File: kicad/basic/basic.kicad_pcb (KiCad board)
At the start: 2 copper layers, 50 x 50 mm, 20 parts, among them P2 CONN_01X15, P3 CONN_01X15, P4 CONN_01X06, P5 CONN_01X01, P6 CONN_01X01, P7 CONN_01X01, P8 CONN_01X01, P9 CONN_01X06, SW1 SW_PUSH, SW2 SW_PUSH

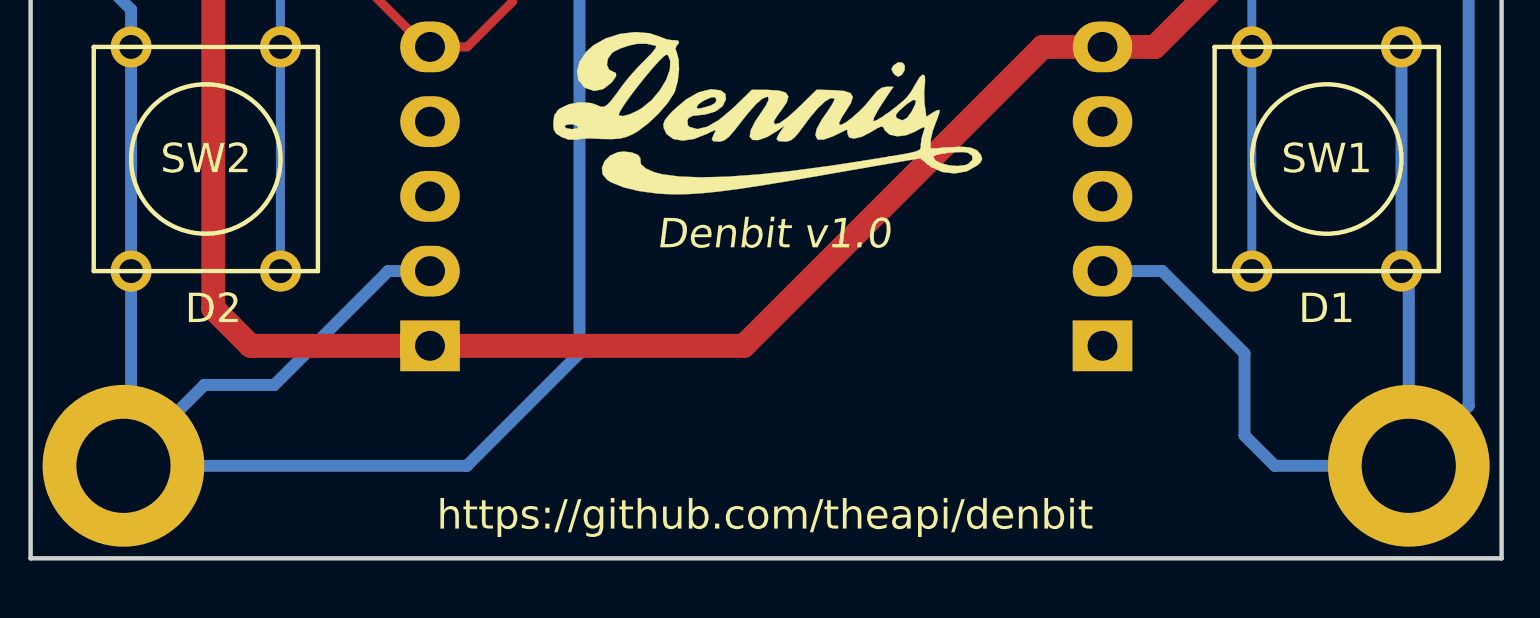
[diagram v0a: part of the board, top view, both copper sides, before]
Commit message: Switch silkscreen labels
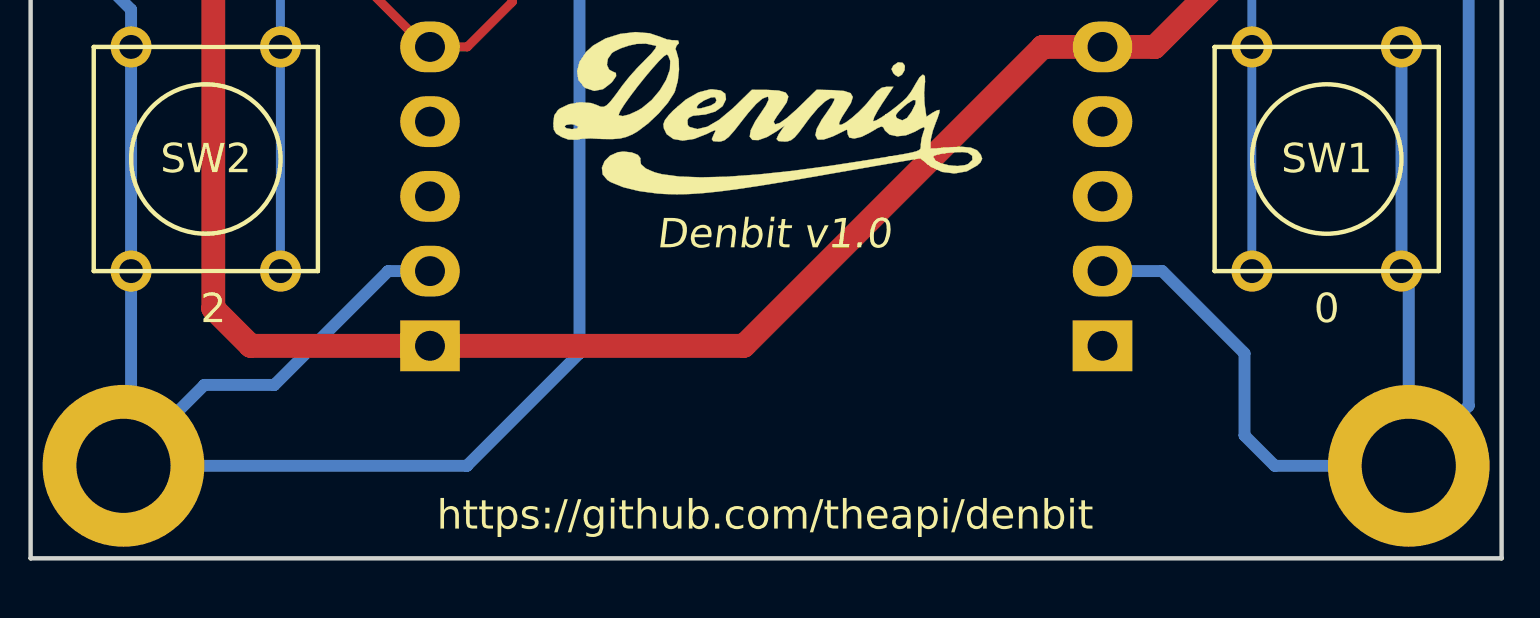
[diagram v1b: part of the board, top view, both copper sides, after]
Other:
- board text added: "0"
- board text added: "2"
- board text removed: "D1"
- board text removed: "D2"
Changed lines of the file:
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@@
     (links 41)
     (no_connects 0)
-    (area 120.251999 71.737999 170.402001 121.888001)
+    (area 115.226999 66.712999 175.427001 126.913001)
     (thickness 1.6)
     (drawings 73)
@@
   (gr_line (start 148.888 72.426) (end 147.872 72.426) (angle 90) (layer B.SilkS) (width 0.2))
   (gr_line (start 148.888 76.998) (end 148.888 72.426) (angle 90) (layer B.SilkS) (width 0.2))
-  (gr_text D2 (at 126.536 113.32) (layer F.SilkS)
+  (gr_text 2 (at 126.536 113.32) (layer F.SilkS)
     (effects (font (size 1 1) (thickness 0.15)))
   )
-  (gr_text D1 (at 164.382 113.32) (layer F.SilkS)
+  (gr_text 0 (at 164.382 113.32) (layer F.SilkS)
     (effects (font (size 1 1) (thickness 0.15)))
   )

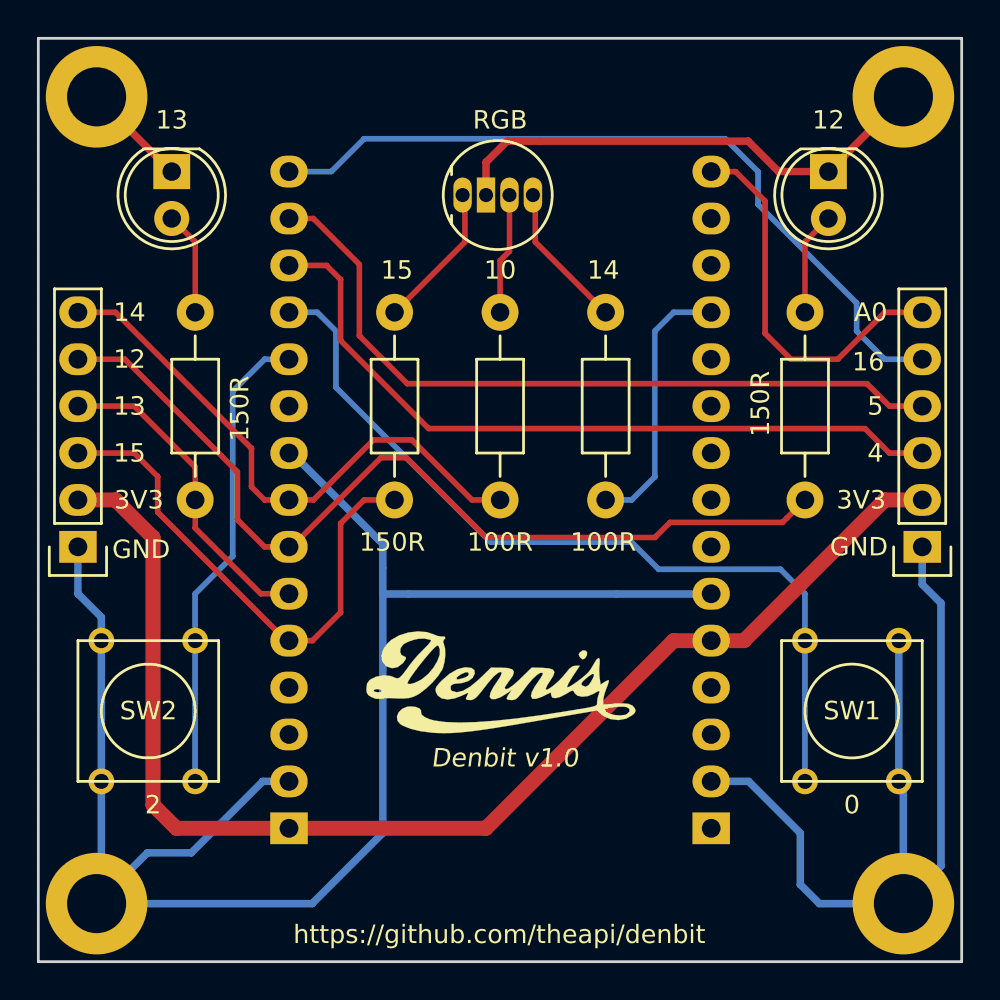
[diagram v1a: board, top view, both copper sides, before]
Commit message: Connect the right switch to the header
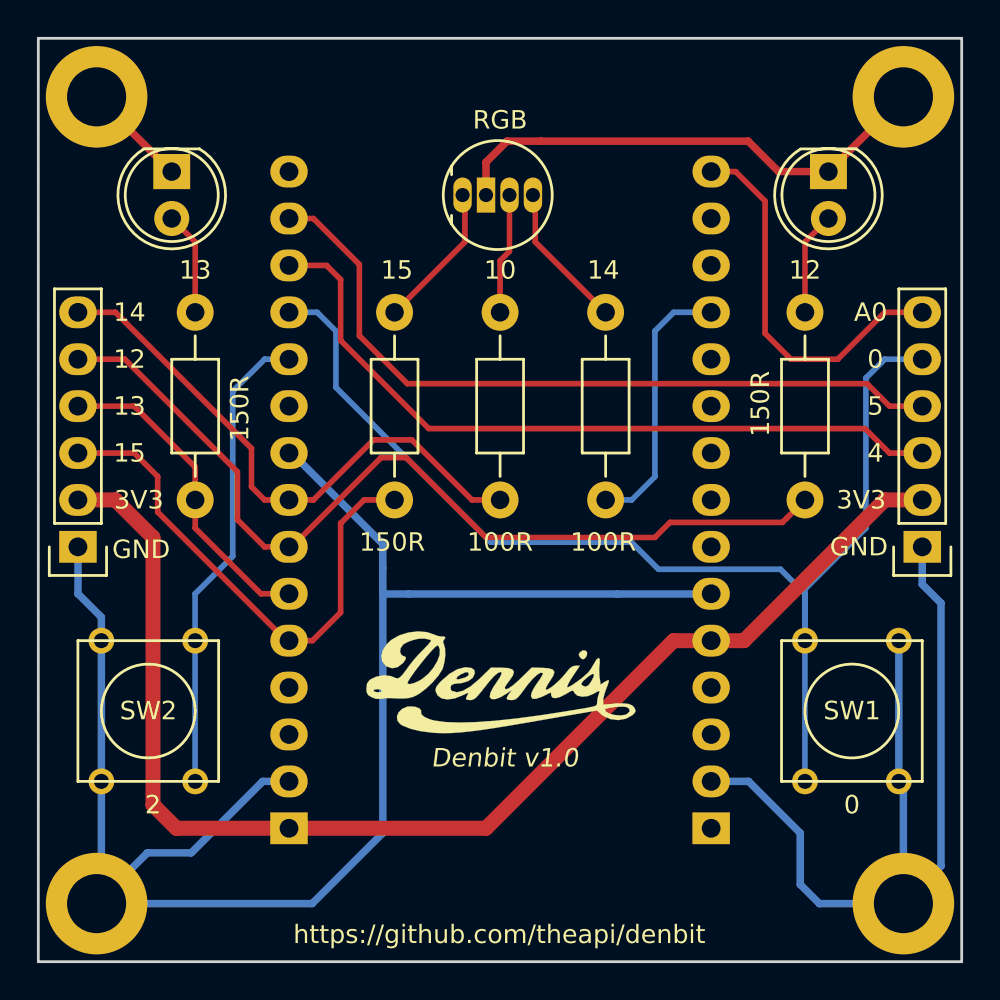
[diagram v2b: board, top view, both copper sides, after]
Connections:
- P4 pad 5: GPIO16 -> GPIO0
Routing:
- net GPIO16: track 41.9 -> 0.00 mm
- net GPIO0: track 46.2 -> 65.3 mm
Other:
- board text removed: "16"
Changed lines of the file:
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@@
     (links 41)
     (no_connects 0)
-    (area 115.226999 66.712999 175.427001 126.913001)
+    (area 120.251999 71.737999 170.402001 121.888001)
     (thickness 1.6)
     (drawings 73)
-    (tracks 165)
+    (tracks 161)
     (zones 0)
     (modules 20)
@@
       (net 29 GPIO5))
     (pad 5 thru_hole oval (at 10.16 0 90) (size 1.7272 2.032) (drill 1.016) (layers *.Cu *.Mask F.SilkS)
-      (net 30 GPIO16))
+      (net 27 GPIO0))
     (pad 6 thru_hole oval (at 12.7 0 90) (size 1.7272 2.032) (drill 1.016) (layers *.Cu *.Mask F.SilkS)
       (net 21 ADC0))
@@
     (effects (font (size 1 1) (thickness 0.15)) (justify mirror))
   )
-  (gr_text 16 (at 165.266 89.332) (layer B.SilkS)
+  (gr_text 0 (at 165.652 89.19) (layer B.SilkS)
     (effects (font (size 1 1) (thickness 0.15)) (justify mirror))
   )
@@
     (effects (font (size 1 1) (thickness 0.15)) (justify mirror))
   )
-  (gr_text 12 (at 163.112 76.236) (layer F.SilkS)
+  (gr_text 12 (at 161.842 84.364) (layer F.SilkS)
     (effects (font (size 1 1) (thickness 0.15)))
   )
@@
     (effects (font (size 1 1) (thickness 0.15)))
   )
-  (gr_text 13 (at 127.552 76.236) (layer F.SilkS)
+  (gr_text 13 (at 128.822 84.364) (layer F.SilkS)
     (effects (font (size 1 1) (thickness 0.15)))
   )
@@
     (effects (font (size 1 1) (thickness 0.15)))
   )
-  (gr_text 16 (at 165.266 89.332) (layer F.SilkS)
+  (gr_text 0 (at 165.652 89.19) (layer F.SilkS)
     (effects (font (size 1 1) (thickness 0.15)))
   )
@@
   (segment (start 128.817 104.445) (end 128.817 112.065) (width 0.305) (layer B.Cu) (net 26))
   (segment (start 128.817 101.905) (end 128.817 104.445) (width 0.305) (layer B.Cu) (net 26))
+  (segment (start 161.842 104.43) (end 161.842 101.636) (width 0.305) (layer B.Cu) (net 27))
+  (segment (start 166.16 89.19) (end 168.192 89.19) (width 0.305) (layer B.Cu) (net 27))
+  (segment (start 165.144 90.206) (end 166.16 89.19) (width 0.305) (layer B.Cu) (net 27))
+  (segment (start 165.144 98.334) (end 165.144 90.206) (width 0.305) (layer B.Cu) (net 27))
+  (segment (start 161.842 101.636) (end 165.144 98.334) (width 0.305) (layer B.Cu) (net 27))
   (segment (start 161.842 101.89) (end 160.51811 100.56611) (width 0.305) (layer B.Cu) (net 27))
   (segment (start 160.51811 100.56611) (end 153.91411 100.56611) (width 0.305) (layer B.Cu) (net 27))
@@
   (segment (start 166.414 91.73) (end 168.192 91.73) (width 0.305) (layer F.Cu) (net 29))
   (segment (start 133.902 81.57) (end 134.0544 81.57) (width 0.305) (layer B.Cu) (net 29))
-  (segment (start 133.902 79.03) (end 136.188 79.03) (width 0.305) (layer B.Cu) (net 30))
-  (segment (start 136.188 79.03) (end 137.966 77.252) (width 0.305) (layer B.Cu) (net 30))
-  (segment (start 137.966 77.252) (end 157.524 77.252) (width 0.305) (layer B.Cu) (net 30))
-  (segment (start 157.524 77.252) (end 159.302 79.03) (width 0.305) (layer B.Cu) (net 30))
-  (segment (start 159.302 79.03) (end 159.302 80.807999) (width 0.305) (layer B.Cu) (net 30))
-  (segment (start 164.636 87.666) (end 166.16 89.19) (width 0.305) (layer B.Cu) (net 30))
-  (segment (start 166.16 89.19) (end 168.192 89.19) (width 0.305) (layer B.Cu) (net 30))
-  (segment (start 159.302 80.807999) (end 164.636 86.141999) (width 0.305) (layer B.Cu) (net 30))
-  (segment (start 164.636 86.141999) (end 164.636 87.666) (width 0.305) (layer B.Cu) (net 30))
   (zone (net 1) (net_name GND) (layer F.Cu) (hatch edge 0.508)
     (connect_pads (clearance 0.508))

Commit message: Use gpio16 instead of gpio0
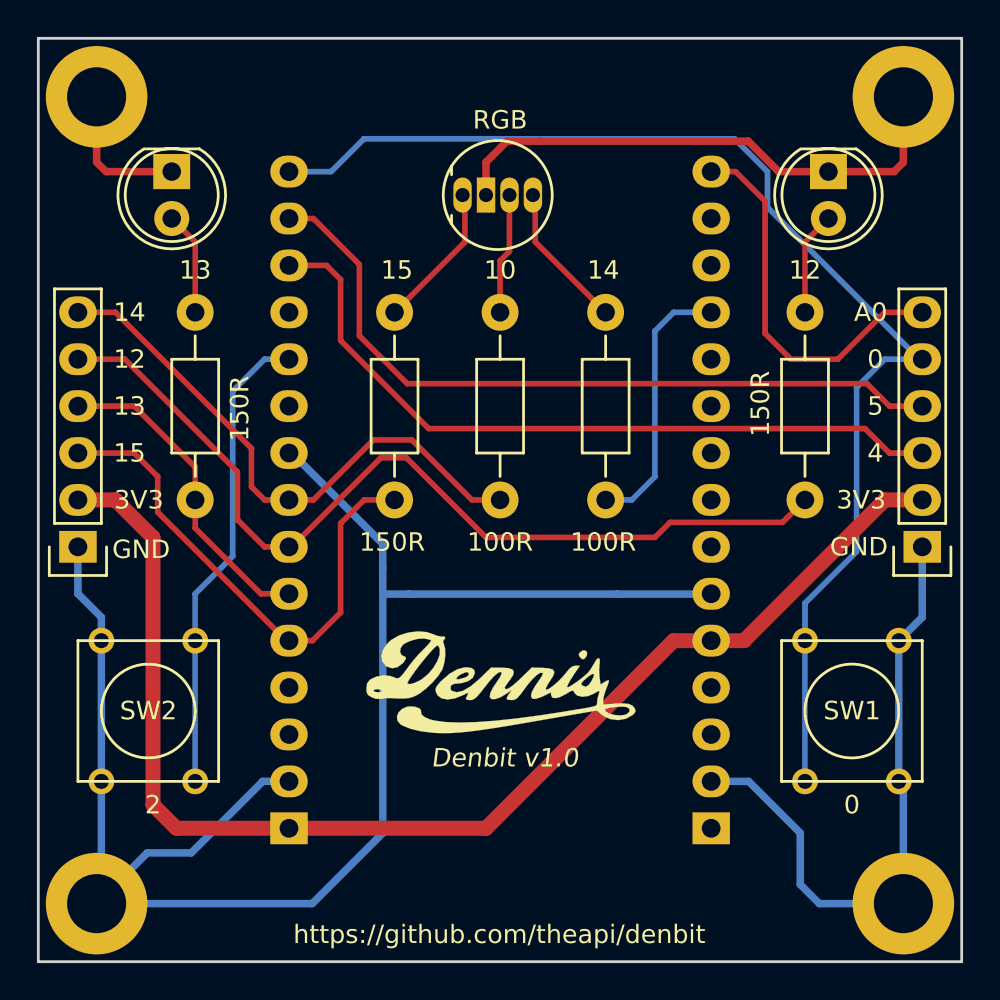
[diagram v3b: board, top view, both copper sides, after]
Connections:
- P4 pad 5: GPIO0 -> GPIO16
- SW1 pad 2: GPIO0 -> GPIO16
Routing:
- net GPIO16: track 0.00 -> 67.8 mm
- net GPIO0: track 65.3 -> 0.00 mm
- net GND: track 175.2 -> 164.4 mm
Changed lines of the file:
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@@
     (links 41)
     (no_connects 0)
-    (area 120.251999 71.737999 170.402001 121.888001)
+    (area 115.226999 66.712999 175.427001 126.913001)
     (thickness 1.6)
     (drawings 73)
@@
       (net 1 GND))
     (pad 2 thru_hole circle (at 3.81 2.54 270) (size 1.397 1.397) (drill 0.8128) (layers *.Cu *.Mask F.SilkS)
-      (net 27 GPIO0))
+      (net 30 GPIO16))
     (pad 1 thru_hole circle (at -3.81 -2.54 270) (size 1.397 1.397) (drill 0.8128) (layers *.Cu *.Mask F.SilkS)
       (net 1 GND))
     (pad 2 thru_hole circle (at -3.81 2.54 270) (size 1.397 1.397) (drill 0.8128) (layers *.Cu *.Mask F.SilkS)
-      (net 27 GPIO0))
+      (net 30 GPIO16))
   )
   (module Buttons_Switches_ThroughHole:SW_PUSH_SMALL (layer F.Cu)
@@
       (net 29 GPIO5))
     (pad 5 thru_hole oval (at 10.16 0 90) (size 1.7272 2.032) (drill 1.016) (layers *.Cu *.Mask F.SilkS)
-      (net 27 GPIO0))
+      (net 30 GPIO16))
     (pad 6 thru_hole oval (at 12.7 0 90) (size 1.7272 2.032) (drill 1.016) (layers *.Cu *.Mask F.SilkS)
       (net 21 ADC0))
@@
   (gr_line (start 170.327 121.813) (end 120.327 121.813) (angle 90) (layer Edge.Cuts) (width 0.15))
   (gr_line (start 170.327 71.813) (end 170.327 121.813) (angle 90) (layer Edge.Cuts) (width 0.15))
+  (segment (start 166.922 104.43) (end 168.192 103.16) (width 0.406) (layer B.Cu) (net 1))
+  (segment (start 168.192 103.16) (end 168.192 99.35) (width 0.406) (layer B.Cu) (net 1))
+  (segment (start 127.552 79.03) (end 123.996 79.03) (width 0.406) (layer F.Cu) (net 1))
+  (segment (start 123.996 79.03) (end 123.483 78.517) (width 0.406) (layer F.Cu) (net 1))
+  (segment (start 123.483 78.517) (end 123.483 74.981) (width 0.406) (layer F.Cu) (net 1))
+  (segment (start 163.112 79.03) (end 166.668 79.03) (width 0.406) (layer F.Cu) (net 1))
+  (segment (start 166.668 79.03) (end 167.171 78.527) (width 0.406) (layer F.Cu) (net 1))
+  (segment (start 167.171 78.527) (end 167.171 74.981) (width 0.406) (layer F.Cu) (net 1))
   (segment (start 166.922 112.05) (end 166.922 104.43) (width 0.406) (layer B.Cu) (net 1))
   (segment (start 167.171 118.669) (end 167.171 112.299) (width 0.406) (layer B.Cu) (net 1))
@@
   (segment (start 145.713 77.379) (end 144.57 78.522) (width 0.406) (layer F.Cu) (net 1))
   (segment (start 163.112 79.03) (end 163.122 79.03) (width 0.406) (layer F.Cu) (net 1))
-  (segment (start 163.122 79.03) (end 167.171 74.981) (width 0.406) (layer F.Cu) (net 1))
   (segment (start 127.552 79.03) (end 127.532 79.03) (width 0.406) (layer F.Cu) (net 1))
-  (segment (start 127.532 79.03) (end 123.483 74.981) (width 0.406) (layer F.Cu) (net 1))
   (segment (start 133.902 94.27) (end 133.7496 94.27) (width 0.406) (layer F.Cu) (net 1))
   (segment (start 123.483 118.669) (end 135.157 118.669) (width 0.406) (layer B.Cu) (net 1))
@@
   (segment (start 151.677 101.905) (end 156.747 101.905) (width 0.406) (layer B.Cu) (net 1))
   (segment (start 156.747 101.905) (end 156.762 101.89) (width 0.406) (layer B.Cu) (net 1))
-  (segment (start 168.192 99.35) (end 168.192 101.382) (width 0.406) (layer B.Cu) (net 1))
-  (segment (start 168.192 101.382) (end 169.208 102.398) (width 0.406) (layer B.Cu) (net 1))
-  (segment (start 169.208 102.398) (end 169.208 116.632) (width 0.406) (layer B.Cu) (net 1))
-  (segment (start 169.208 116.632) (end 167.171 118.669) (width 0.406) (layer B.Cu) (net 1))
   (segment (start 133.902 94.27) (end 134.0544 94.27) (width 0.406) (layer B.Cu) (net 1))
   (segment (start 134.0544 94.27) (end 138.977 99.1926) (width 0.406) (layer B.Cu) (net 1))
@@
   (segment (start 128.817 104.445) (end 128.817 112.065) (width 0.305) (layer B.Cu) (net 26))
   (segment (start 128.817 101.905) (end 128.817 104.445) (width 0.305) (layer B.Cu) (net 26))
-  (segment (start 161.842 104.43) (end 161.842 101.636) (width 0.305) (layer B.Cu) (net 27))
-  (segment (start 166.16 89.19) (end 168.192 89.19) (width 0.305) (layer B.Cu) (net 27))
-  (segment (start 165.144 90.206) (end 166.16 89.19) (width 0.305) (layer B.Cu) (net 27))
-  (segment (start 165.144 98.334) (end 165.144 90.206) (width 0.305) (layer B.Cu) (net 27))
-  (segment (start 161.842 101.636) (end 165.144 98.334) (width 0.305) (layer B.Cu) (net 27))
-  (segment (start 161.842 101.89) (end 160.51811 100.56611) (width 0.305) (layer B.Cu) (net 27))
-  (segment (start 160.51811 100.56611) (end 153.91411 100.56611) (width 0.305) (layer B.Cu) (net 27))
-  (segment (start 153.91411 100.56611) (end 152.444 99.096) (width 0.305) (layer B.Cu) (net 27))
-  (segment (start 144.824 99.096) (end 136.442 90.714) (width 0.305) (layer B.Cu) (net 27))
-  (segment (start 152.444 99.096) (end 144.824 99.096) (width 0.305) (layer B.Cu) (net 27))
-  (segment (start 136.442 90.714) (end 136.442 87.666) (width 0.305) (layer B.Cu) (net 27))
-  (segment (start 136.442 87.666) (end 135.426 86.65) (width 0.305) (layer B.Cu) (net 27))
-  (segment (start 135.426 86.65) (end 133.902 86.65) (width 0.305) (layer B.Cu) (net 27))
-  (segment (start 161.837 104.445) (end 161.837 112.065) (width 0.305) (layer B.Cu) (net 27))
-  (segment (start 161.837 101.905) (end 161.837 104.445) (width 0.305) (layer B.Cu) (net 27))
   (segment (start 133.902 84.11) (end 135.934 84.11) (width 0.305) (layer F.Cu) (net 28))
   (segment (start 135.934 84.11) (end 136.696 84.872) (width 0.305) (layer F.Cu) (net 28))
@@
   (segment (start 166.414 91.73) (end 168.192 91.73) (width 0.305) (layer F.Cu) (net 29))
   (segment (start 133.902 81.57) (end 134.0544 81.57) (width 0.305) (layer B.Cu) (net 29))
+  (segment (start 133.902 79.03) (end 136.188 79.03) (width 0.305) (layer B.Cu) (net 30))
+  (segment (start 158.032 77.252) (end 159.81 79.03) (width 0.305) (layer B.Cu) (net 30))
+  (segment (start 136.188 79.03) (end 137.966 77.252) (width 0.305) (layer B.Cu) (net 30))
+  (segment (start 137.966 77.252) (end 158.032 77.252) (width 0.305) (layer B.Cu) (net 30))
+  (segment (start 159.81 79.03) (end 159.81 80.9604) (width 0.305) (layer B.Cu) (net 30))
+  (segment (start 159.81 80.9604) (end 168.0396 89.19) (width 0.305) (layer B.Cu) (net 30))
+  (segment (start 168.0396 89.19) (end 168.192 89.19) (width 0.305) (layer B.Cu) (net 30))
+  (segment (start 161.842 104.43) (end 161.842 102.398) (width 0.305) (layer B.Cu) (net 30))
+  (segment (start 161.842 102.398) (end 164.636 99.604) (width 0.305) (layer B.Cu) (net 30))
+  (segment (start 164.636 90.714) (end 166.16 89.19) (width 0.305) (layer B.Cu) (net 30))
+  (segment (start 164.636 99.604) (end 164.636 90.714) (width 0.305) (layer B.Cu) (net 30))
+  (segment (start 166.16 89.19) (end 168.192 89.19) (width 0.305) (layer B.Cu) (net 30))
+  (segment (start 161.837 104.445) (end 161.837 112.065) (width 0.305) (layer B.Cu) (net 30))
   (zone (net 1) (net_name GND) (layer F.Cu) (hatch edge 0.508)
     (connect_pads (clearance 0.508))
